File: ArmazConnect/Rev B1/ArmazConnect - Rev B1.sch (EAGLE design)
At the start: 40 parts, among them X0 NC3FAAV2, X1 NC3FAAV2, X2 NC3FAAV2, X3 NC3FAAV2, X4 NC5FAV-SW, X5 NC5MAV-SW, X6 NC5FAV-SW, X7 5504F1-09S-02A-03, X8 87832-26

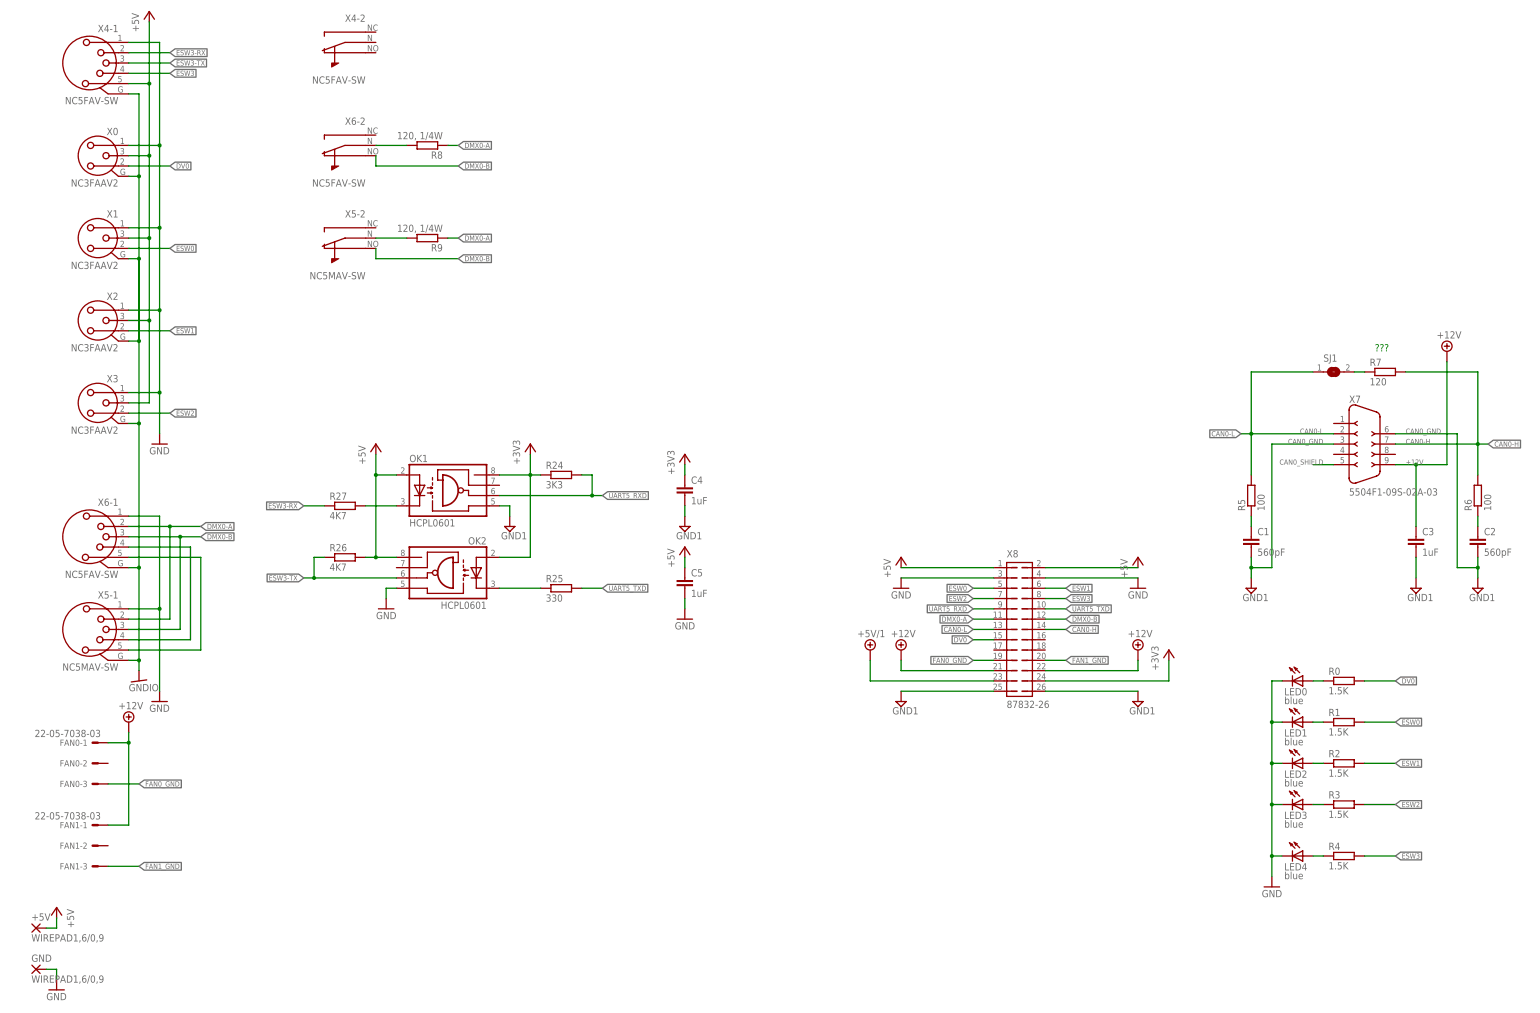
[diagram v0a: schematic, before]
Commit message: Add 84102C to murata inductance library, add MEE3 to dc/dc converter library, update of ArmazConnect rev B1 (dc/dc 12V to 5V), create Varmo Eagles project
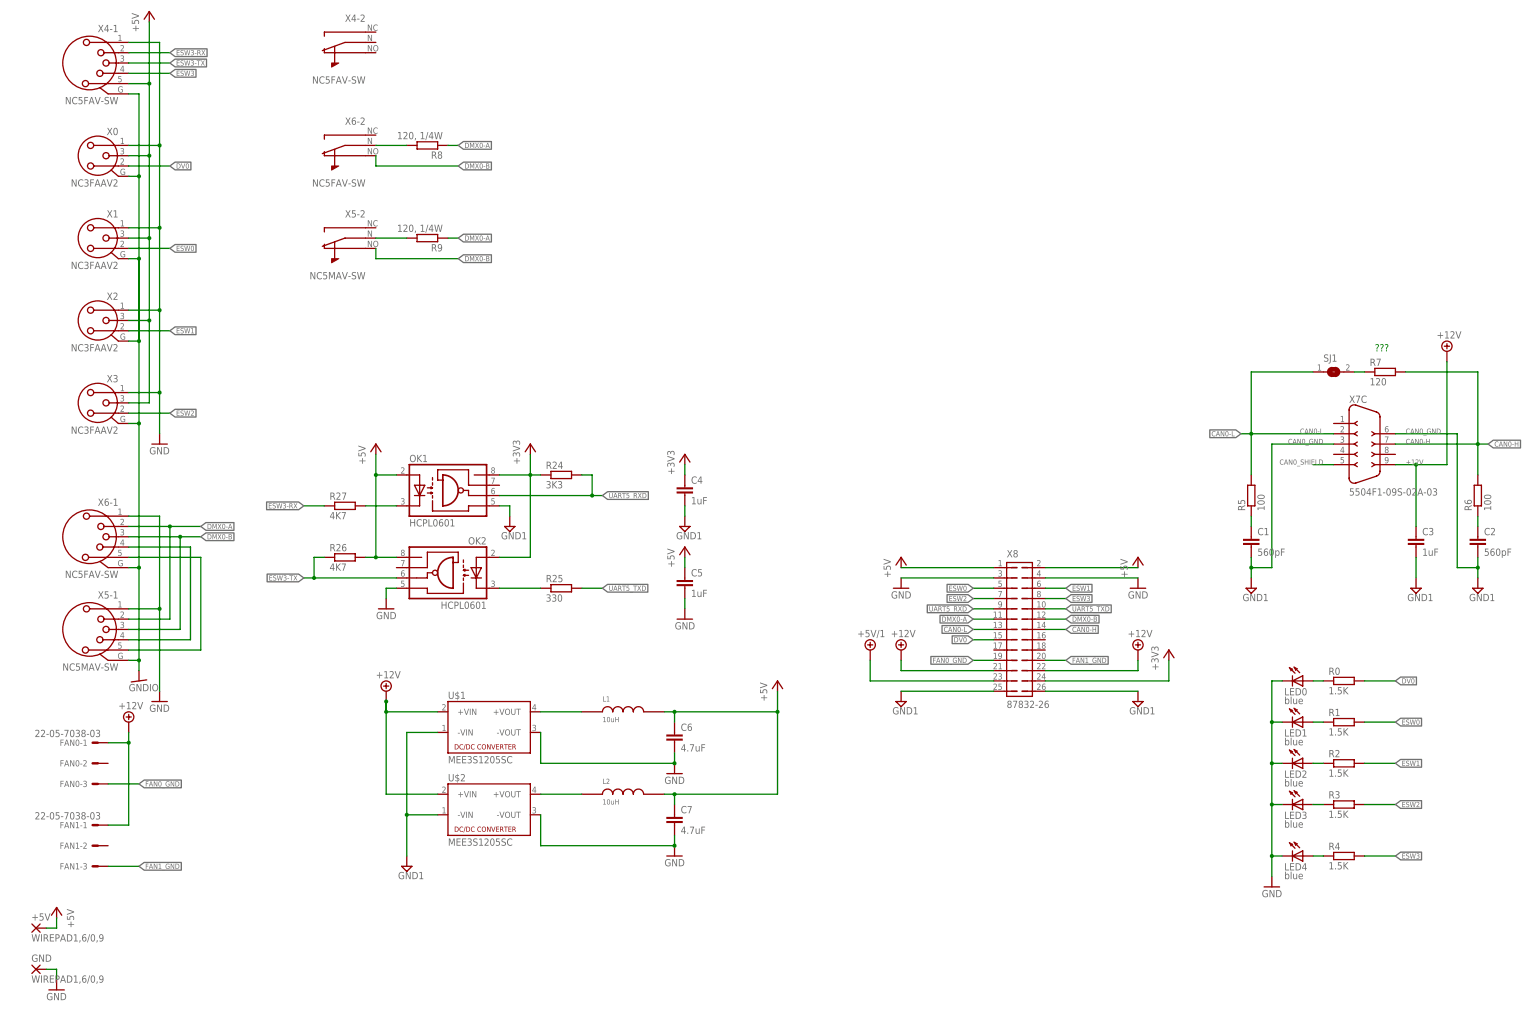
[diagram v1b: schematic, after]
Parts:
- added C6, C7: 4.7uF, rcl:C-EUC0603
- added L1, L2: 10uH, murata-inductance:84103C
- added U$1, U$2: MEE3S1205SC, dc-dc-converter:MEE3S1205SC
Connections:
- new net N$10: L2.1, U$2.+VOUT
- new net N$9: L1.1, U$1.+VOUT
- net +12V: now also U$1.+VIN, U$2.+VIN, X7C.9; no longer X7.9
- net +5V: now also C6.1, C7.1, L1.2, L2.2
- net CAN0-H: now also X7C.7; no longer X7.7
- net CAN0-L: now also X7C.2; no longer X7.2
- net CAN0_GND: now also X7C.3, X7C.6; no longer X7.3, X7.6
- net CAN0_SHIELD: now also X7C.5; no longer X7.5
- net GND: now also C6.2, C7.2, U$1.-VOUT, U$2.-VOUT
- net GND1: now also U$1.-VIN, U$2.-VIN
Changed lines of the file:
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@@
 <part name="+3V2" library="supply1" deviceset="+3V3" device=""/>
 <part name="+3V3" library="supply1" deviceset="+3V3" device=""/>
+<part name="U$1" library="dc-dc-converter" deviceset="MEE3" device="" technology="S1205SC"/>
+<part name="U$2" library="dc-dc-converter" deviceset="MEE3" device="" technology="S1205SC"/>
+<part name="SUPPLY13" library="supply2" deviceset="+12V" device=""/>
+<part name="SUPPLY14" library="supply2" deviceset="GND1" device=""/>
+<part name="L2" library="murata-inductance" deviceset="84103C" device="" value="10uH"/>
+<part name="L1" library="murata-inductance" deviceset="84103C" device="" value="10uH"/>
+<part name="C6" library="rcl" deviceset="C-EU" device="C0603" value="4.7uF"/>
+<part name="C7" library="rcl" deviceset="C-EU" device="C0603" value="4.7uF"/>
+<part name="GND3" library="supply1" deviceset="GND" device=""/>
+<part name="GND4" library="supply1" deviceset="GND" device=""/>
+<part name="P+4" library="supply1" deviceset="+5V" device=""/>
 </parts>
 <sheets>
@@
 <instance part="X5" gate="-1" x="22.86" y="99.06" rot="MR0"/>
 <instance part="GND13" gate="1" x="38.1" y="144.78"/>
-<instance part="X7" gate="G$1" x="335.28" y="144.78">
+<instance part="X7" gate="C" x="335.28" y="144.78">
 <attribute name="OC_FARNELL" x="335.28" y="144.78" size="1.27" layer="96" display="off"/>
 <attribute name="MF" x="335.28" y="144.78" size="1.27" layer="96" display="off"/>
@@
 <instance part="+3V2" gate="G$1" x="129.54" y="144.78"/>
 <instance part="+3V3" gate="G$1" x="167.64" y="142.24"/>
+<instance part="U$1" gate="G$1" x="119.38" y="76.2"/>
+<instance part="U$2" gate="G$1" x="119.38" y="55.88"/>
+<instance part="SUPPLY13" gate="+12V" x="93.98" y="83.82"/>
+<instance part="SUPPLY14" gate="G$1" x="99.06" y="40.64"/>
+<instance part="L2" gate="L$1" x="152.4" y="58.42"/>
+<instance part="L1" gate="L$1" x="152.4" y="78.74"/>
+<instance part="C6" gate="G$1" x="165.1" y="73.66"/>
+<instance part="C7" gate="G$1" x="165.1" y="53.34"/>
+<instance part="GND3" gate="1" x="165.1" y="63.5" rot="MR0"/>
+<instance part="GND4" gate="1" x="165.1" y="43.18" rot="MR0"/>
+<instance part="P+4" gate="1" x="190.5" y="86.36"/>
 </instances>
 <busses>
@@
 <wire x1="167.64" y1="104.14" x2="167.64" y2="106.68" width="0.1524" layer="91"/>
 </segment>
+<segment>
+<pinref part="C6" gate="G$1" pin="2"/>
+<pinref part="GND3" gate="1" pin="GND"/>
+<pinref part="U$1" gate="G$1" pin="-VOUT"/>
+<wire x1="165.1" y1="66.04" x2="132.08" y2="66.04" width="0.1524" layer="91"/>
+<wire x1="132.08" y1="66.04" x2="132.08" y2="73.66" width="0.1524" layer="91"/>
+<wire x1="165.1" y1="66.04" x2="165.1" y2="68.58" width="0.1524" layer="91"/>
+<junction x="165.1" y="66.04"/>
+</segment>
+<segment>
+<pinref part="C7" gate="G$1" pin="2"/>
+<pinref part="GND4" gate="1" pin="GND"/>
+<pinref part="U$2" gate="G$1" pin="-VOUT"/>
+<wire x1="132.08" y1="53.34" x2="132.08" y2="45.72" width="0.1524" layer="91"/>
+<wire x1="132.08" y1="45.72" x2="165.1" y2="45.72" width="0.1524" layer="91"/>
+<wire x1="165.1" y1="45.72" x2="165.1" y2="48.26" width="0.1524" layer="91"/>
+<junction x="165.1" y="45.72"/>
+</segment>
 </net>
 <net name="N$27" class="0">
@@
 <wire x1="167.64" y1="116.84" x2="167.64" y2="114.3" width="0.1524" layer="91"/>
 </segment>
+<segment>
+<pinref part="L2" gate="L$1" pin="2"/>
+<pinref part="C7" gate="G$1" pin="1"/>
+<wire x1="162.56" y1="58.42" x2="165.1" y2="58.42" width="0.1524" layer="91"/>
+<wire x1="165.1" y1="58.42" x2="165.1" y2="55.88" width="0.1524" layer="91"/>
+<wire x1="165.1" y1="58.42" x2="190.5" y2="58.42" width="0.1524" layer="91"/>
+<wire x1="190.5" y1="58.42" x2="190.5" y2="78.74" width="0.1524" layer="91"/>
+<pinref part="P+4" gate="1" pin="+5V"/>
+<pinref part="C6" gate="G$1" pin="1"/>
+<pinref part="L1" gate="L$1" pin="2"/>
+<wire x1="190.5" y1="78.74" x2="190.5" y2="83.82" width="0.1524" layer="91"/>
+<wire x1="162.56" y1="78.74" x2="165.1" y2="78.74" width="0.1524" layer="91"/>
+<wire x1="165.1" y1="78.74" x2="165.1" y2="76.2" width="0.1524" layer="91"/>
+<wire x1="165.1" y1="78.74" x2="190.5" y2="78.74" width="0.1524" layer="91"/>
+<junction x="165.1" y="78.74"/>
+<junction x="165.1" y="58.42"/>
+<junction x="190.5" y="78.74"/>
+</segment>
 </net>
 <net name="ESW0" class="0">
@@
 <net name="CAN0-L" class="0">
 <segment>
-<pinref part="X7" gate="G$1" pin="2"/>
+<pinref part="X7" gate="C" pin="2"/>
 <label x="325.12" y="147.32" size="1.27" layer="95" rot="MR0"/>
 <wire x1="327.66" y1="147.32" x2="307.34" y2="147.32" width="0.1524" layer="91"/>
@@
 <net name="CAN0-H" class="0">
 <segment>
-<pinref part="X7" gate="G$1" pin="7"/>
+<pinref part="X7" gate="C" pin="7"/>
 <label x="345.44" y="144.78" size="1.27" layer="95"/>
 <wire x1="342.9" y1="144.78" x2="363.22" y2="144.78" width="0.1524" layer="91"/>
@@
 <net name="+12V" class="1">
 <segment>
-<pinref part="X7" gate="G$1" pin="9"/>
+<pinref part="X7" gate="C" pin="9"/>
 <wire x1="342.9" y1="139.7" x2="347.98" y2="139.7" width="0.1524" layer="91"/>
 <label x="345.44" y="139.7" size="1.27" layer="95"/>
@@
 <junction x="30.48" y="71.12"/>
 </segment>
+<segment>
+<pinref part="U$1" gate="G$1" pin="+VIN"/>
+<pinref part="SUPPLY13" gate="+12V" pin="+12V"/>
+<wire x1="106.68" y1="78.74" x2="93.98" y2="78.74" width="0.1524" layer="91"/>
+<wire x1="93.98" y1="78.74" x2="93.98" y2="81.28" width="0.1524" layer="91"/>
+<wire x1="93.98" y1="81.28" x2="93.98" y2="78.74" width="0.1524" layer="91"/>
+<pinref part="U$2" gate="G$1" pin="+VIN"/>
+<wire x1="93.98" y1="78.74" x2="93.98" y2="58.42" width="0.1524" layer="91"/>
+<wire x1="93.98" y1="58.42" x2="106.68" y2="58.42" width="0.1524" layer="91"/>
+<junction x="93.98" y="78.74"/>
+<junction x="93.98" y="81.28"/>
+</segment>
 </net>
 <net name="GND1" class="1">
@@
 <pinref part="SUPPLY12" gate="G$1" pin="GND1"/>
 <wire x1="167.64" y1="127" x2="167.64" y2="129.54" width="0.1524" layer="91"/>
+</segment>
+<segment>
+<pinref part="U$1" gate="G$1" pin="-VIN"/>
+<pinref part="SUPPLY14" gate="G$1" pin="GND1"/>
+<wire x1="106.68" y1="73.66" x2="99.06" y2="73.66" width="0.1524" layer="91"/>
+<wire x1="99.06" y1="73.66" x2="99.06" y2="53.34" width="0.1524" layer="91"/>
+<wire x1="99.06" y1="43.18" x2="99.06" y2="53.34" width="0.1524" layer="91"/>
+<pinref part="U$2" gate="G$1" pin="-VIN"/>
+<wire x1="99.06" y1="53.34" x2="106.68" y2="53.34" width="0.1524" layer="91"/>
+<junction x="99.06" y="53.34"/>
 </segment>
 </net>
@@
 <net name="CAN0_SHIELD" class="0">
 <segment>
-<pinref part="X7" gate="G$1" pin="5"/>
+<pinref part="X7" gate="C" pin="5"/>
 <wire x1="327.66" y1="139.7" x2="322.58" y2="139.7" width="0.1524" layer="91"/>
 <label x="325.12" y="139.7" size="1.27" layer="95" rot="MR0"/>
@@
 <net name="CAN0_GND" class="0">
 <segment>
-<pinref part="X7" gate="G$1" pin="3"/>
+<pinref part="X7" gate="C" pin="3"/>
 <label x="325.12" y="144.78" size="1.27" layer="95" rot="MR0"/>
 <wire x1="327.66" y1="144.78" x2="312.42" y2="144.78" width="0.1524" layer="91"/>
@@
 </segment>
 <segment>
-<pinref part="X7" gate="G$1" pin="6"/>
+<pinref part="X7" gate="C" pin="6"/>
 <label x="345.44" y="147.32" size="1.27" layer="95"/>
 <wire x1="342.9" y1="147.32" x2="358.14" y2="147.32" width="0.1524" layer="91"/>
@@
 </segment>
 </net>
+<net name="N$9" class="0">
+<segment>
+<pinref part="U$1" gate="G$1" pin="+VOUT"/>
+<wire x1="132.08" y1="78.74" x2="142.24" y2="78.74" width="0.1524" layer="91"/>
+<pinref part="L1" gate="L$1" pin="1"/>
+</segment>
+</net>
+<net name="N$10" class="0">
+<segment>
+<pinref part="U$2" gate="G$1" pin="+VOUT"/>
+<wire x1="132.08" y1="58.42" x2="142.24" y2="58.42" width="0.1524" layer="91"/>
+<pinref part="L2" gate="L$1" pin="1"/>
+</segment>
+</net>
